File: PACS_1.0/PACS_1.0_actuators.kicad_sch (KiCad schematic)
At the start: 0 parts

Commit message: Finished water pump, cleaned out empty sheets, added details in 'post its'
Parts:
- added D1: GS1M-LTP, symbol Device:D
- added J2: Conn_01x02_Pin, symbol Connector:Conn_01x02_Pin
- added Q2: ~, symbol AOSS32334C:AOSS32334C
- added R4: 1k, symbol Device:R
- added R5: 10k, symbol Device:R
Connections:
- new net: Q2.1, R4.2
- new net: D1.2 (A), J2.1 (Pin_1), Q2.3
- new net +3.3V: D1.1 (K), J2.2 (Pin_2)
- new net GND: Q2.2, R5.1
- new net PWM: R4.1, R5.2
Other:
- note added: "Water Pump Connection"
- company: PACS -> (none)

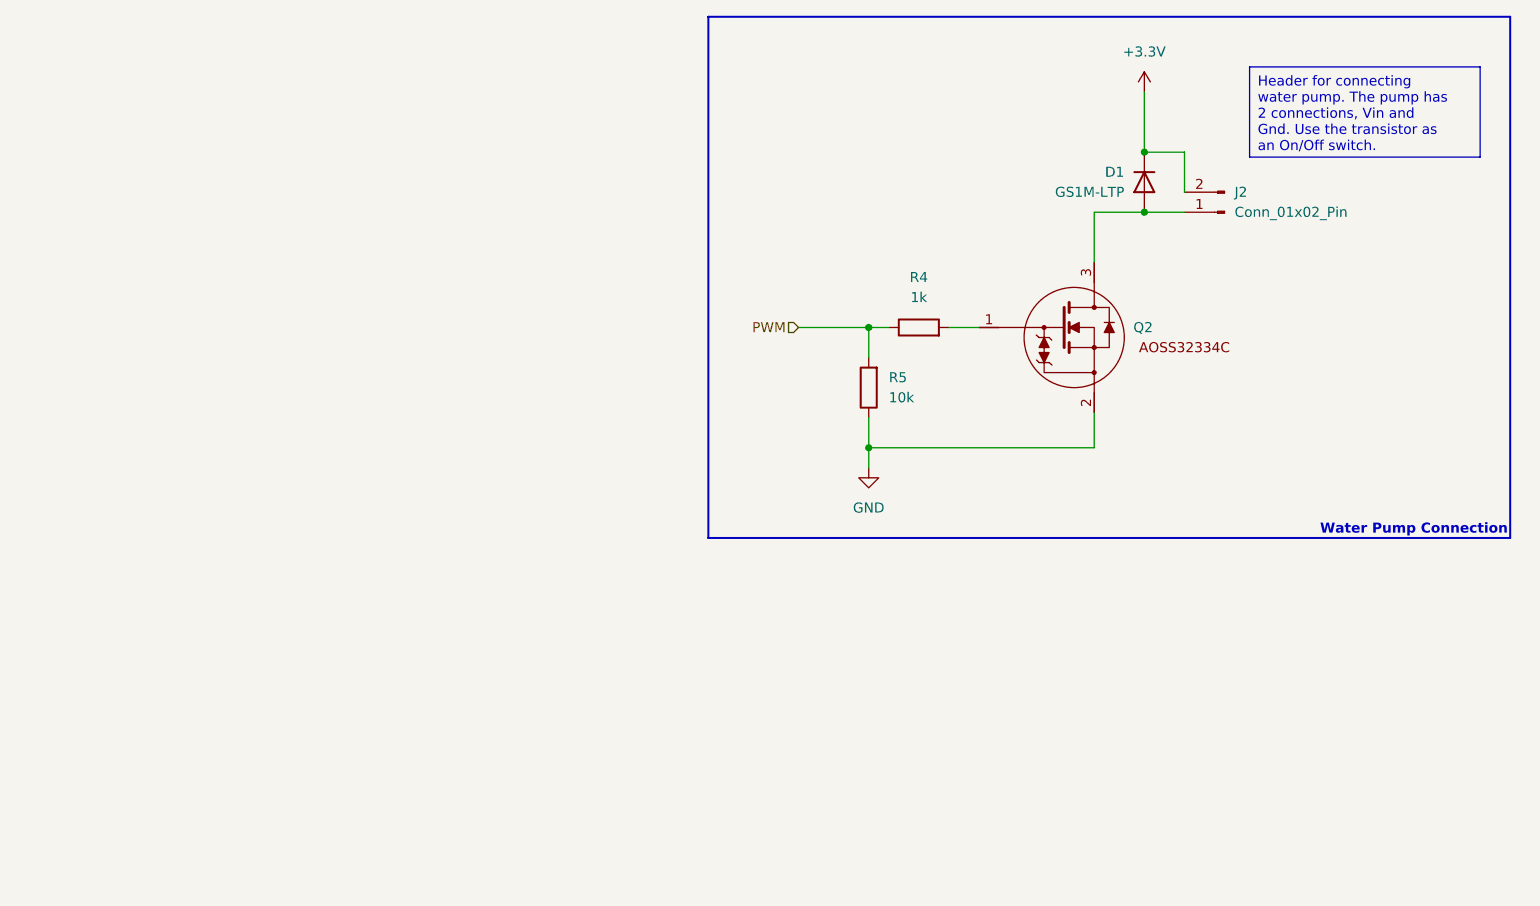
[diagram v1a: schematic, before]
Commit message: Finished Zigbee Module
also fixed some library issues
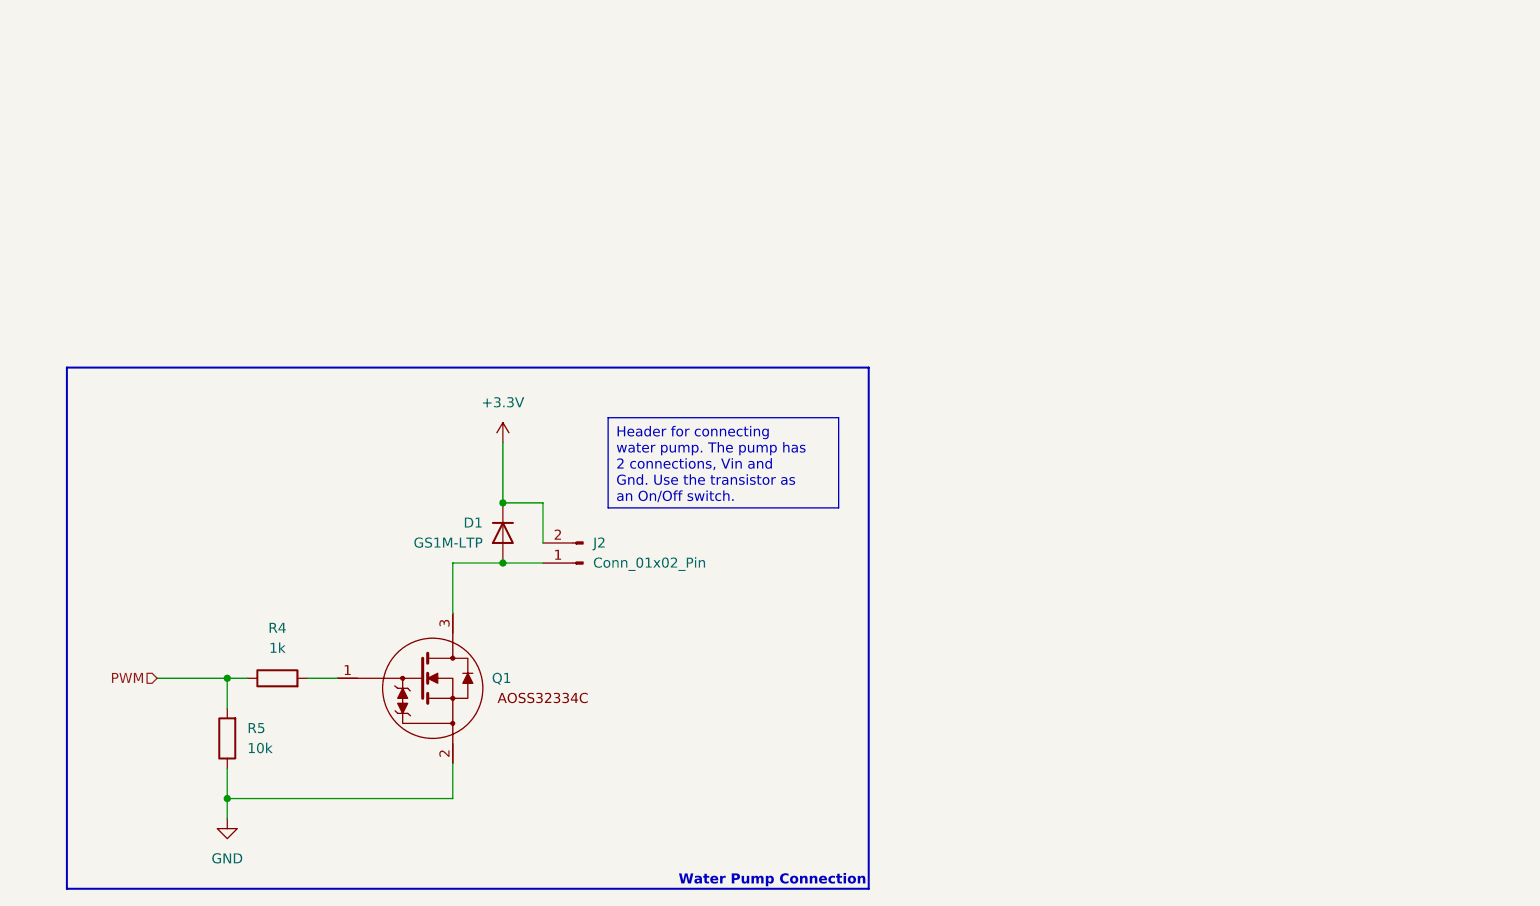
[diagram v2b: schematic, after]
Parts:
- renumbered Q2 to Q1
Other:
- moved on the sheet: D1, J2, Q1, R4, R5

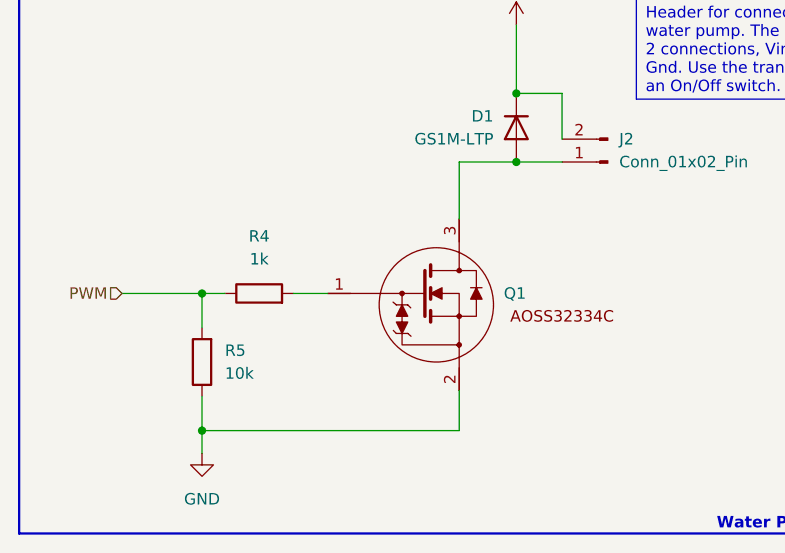
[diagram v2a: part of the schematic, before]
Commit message: Added Undervoltage Protection, removed LED kicad
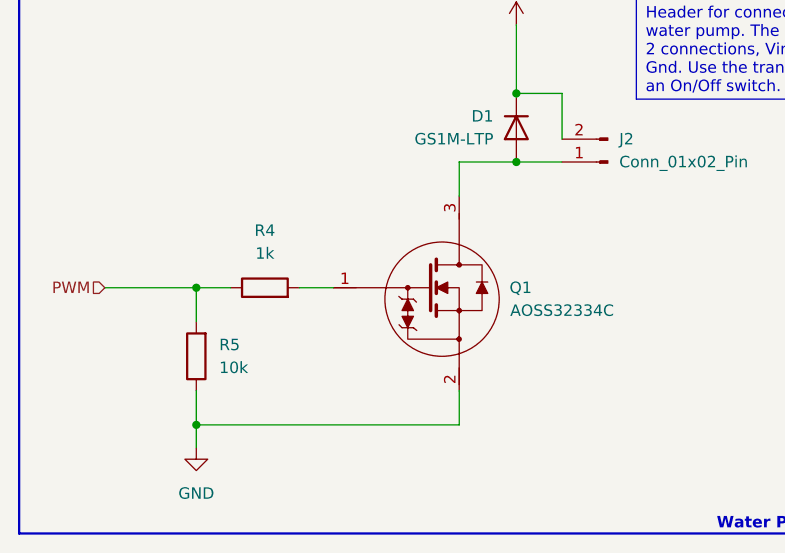
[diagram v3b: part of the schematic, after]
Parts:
- Q1: footprint (none) -> Package_TO_SOT_SMD:TSOT-23; Ref Name (none) -> AOSS32334C
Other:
- moved on the sheet: R4, R5
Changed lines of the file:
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@@
 	(paper "A4")
+	(junction
+		(at 111.76 115.57)
+		(diameter 0)
+		(color 0 0 0 0)
+	)
 	(junction
 		(at 147.32 86.36)
@@
 	)
 	(junction
-		(at 112.395 100.965)
-		(diameter 0)
-		(color 0 0 0 0)
-	)
-	(junction
 		(at 147.32 78.74)
 		(diameter 0)
@@
 	)
 	(junction
-		(at 112.395 116.205)
+		(at 111.76 100.33)
 		(diameter 0)
 		(color 0 0 0 0)
@@
 	(wire
 		(pts
-			(xy 112.395 116.205) (xy 140.97 116.205)
+			(xy 123.19 100.33) (xy 127 100.33)
 		)
 		(stroke
@@
 	(wire
 		(pts
-			(xy 140.97 86.36) (xy 140.97 92.71)
-		)
-		(stroke
-			(width 0)
-			(type default)
-		)
-	)
-	(wire
-		(pts
-			(xy 112.395 112.395) (xy 112.395 116.205)
+			(xy 111.76 115.57) (xy 140.97 115.57)
+		)
+		(stroke
+			(width 0)
+			(type default)
+		)
+	)
+	(wire
+		(pts
+			(xy 111.76 115.57) (xy 111.76 118.11)
 		)
 		(stroke
@@
 	(wire
 		(pts
-			(xy 112.395 100.965) (xy 114.935 100.965)
-		)
-		(stroke
-			(width 0)
-			(type default)
-		)
-	)
-	(wire
-		(pts
-			(xy 122.555 100.965) (xy 126.365 100.965)
-		)
-		(stroke
-			(width 0)
-			(type default)
-		)
-	)
-	(wire
-		(pts
-			(xy 103.505 100.965) (xy 112.395 100.965)
-		)
-		(stroke
-			(width 0)
-			(type default)
-		)
-	)
-	(wire
-		(pts
-			(xy 140.97 111.76) (xy 140.97 116.205)
+			(xy 101.6 100.33) (xy 111.76 100.33)
+		)
+		(stroke
+			(width 0)
+			(type default)
+		)
+	)
+	(wire
+		(pts
+			(xy 140.97 86.36) (xy 140.97 90.17)
+		)
+		(stroke
+			(width 0)
+			(type default)
+		)
+	)
+	(wire
+		(pts
+			(xy 140.97 111.76) (xy 140.97 115.57)
 		)
 		(stroke
@@
 	(wire
 		(pts
-			(xy 112.395 100.965) (xy 112.395 104.775)
-		)
-		(stroke
-			(width 0)
-			(type default)
-		)
-	)
-	(wire
-		(pts
-			(xy 112.395 116.205) (xy 112.395 118.745)
+			(xy 111.76 100.33) (xy 111.76 104.14)
+		)
+		(stroke
+			(width 0)
+			(type default)
+		)
+	)
+	(wire
+		(pts
+			(xy 111.76 111.76) (xy 111.76 115.57)
+		)
+		(stroke
+			(width 0)
+			(type default)
+		)
+	)
+	(wire
+		(pts
+			(xy 111.76 100.33) (xy 115.57 100.33)
 		)
 		(stroke
@@
 	(hierarchical_label "PWM"
 		(shape input)
-		(at 103.505 100.965 180)
+		(at 101.6 100.33 180)
 		(fields_autoplaced yes)
 		(effects
@@
 	(symbol
 		(lib_id "Device:R")
-		(at 112.395 108.585 180)
+		(at 111.76 107.95 180)
 		(unit 1)
 		(exclude_from_sim no)
@@
 		(fields_autoplaced yes)
 		(property "Reference" "R5"
-			(at 114.935 107.3149 0)
+			(at 114.3 106.6799 0)
 			(effects
 				(font
@@
 		)
 		(property "Value" "10k"
-			(at 114.935 109.8549 0)
+			(at 114.3 109.2199 0)
 			(effects
 				(font
@@
 		)
 		(property "Footprint" ""
-			(at 114.173 108.585 90)
+			(at 113.538 107.95 90)
 			(effects
 				(font
@@
 		)
 		(property "Datasheet" "~"
-			(at 112.395 108.585 0)
+			(at 111.76 107.95 0)
 			(effects
 				(font
@@
 		)
 		(property "Description" "Resistor"
-			(at 112.395 108.585 0)
+			(at 111.76 107.95 0)
 			(effects
 				(font
@@
 	(symbol
 		(lib_id "Device:R")
-		(at 118.745 100.965 90)
+		(at 119.38 100.33 90)
 		(unit 1)
 		(exclude_from_sim no)
@@
 		(fields_autoplaced yes)
 		(property "Reference" "R4"
-			(at 118.745 94.615 90)
+			(at 119.38 93.98 90)
 			(effects
 				(font
@@
 		)
 		(property "Value" "1k"
-			(at 118.745 97.155 90)
+			(at 119.38 96.52 90)
 			(effects
 				(font
@@
 		)
 		(property "Footprint" ""
-			(at 118.745 102.743 90)
+			(at 119.38 102.108 90)
 			(effects
 				(font
@@
 		)
 		(property "Datasheet" "~"
-			(at 118.745 100.965 0)
+			(at 119.38 100.33 0)
 			(effects
 				(font
@@
 		)
 		(property "Description" "Resistor"
-			(at 118.745 100.965 0)
+			(at 119.38 100.33 0)
 			(effects
 				(font
@@
 	(symbol
 		(lib_id "AOSS32334C:AOSS32334C")
-		(at 146.685 100.965 0)
+		(at 147.32 100.33 0)
 		(unit 1)
 		(exclude_from_sim no)
@@
 		(dnp no)
 		(property "Reference" "Q1"
-			(at 145.923 100.965 0)
+			(at 146.558 100.33 0)
 			(effects
 				(font
@@
 		)
 		(property "Value" "~"
-			(at 159.385 103.505 0)
+			(at 160.02 102.87 0)
 			(effects
 				(font
@@
 			)
 		)
-		(property "Footprint" ""
-			(at 146.685 100.965 0)
+		(property "Footprint" "Package_TO_SOT_SMD:TSOT-23"
+			(at 147.32 100.33 0)
 			(effects
 				(font
@@
 		)
 		(property "Datasheet" ""
-			(at 146.685 100.965 0)
+			(at 147.32 100.33 0)
 			(effects
 				(font
@@
 		)
 		(property "Description" ""
-			(at 146.685 100.965 0)
-			(effects
-				(font
-					(size 1.27 1.27)
-				)
-				(hide yes)
+			(at 147.32 100.33 0)
+			(effects
+				(font
+					(size 1.27 1.27)
+				)
+				(hide yes)
+			)
+		)
+		(property "Ref Name" "AOSS32334C"
+			(at 152.4 102.87 0)
+			(effects
+				(font
+					(size 1.27 1.27)
+					(color 0 72 72 1)
+				)
 			)
 		)
@@
 	(symbol
 		(lib_id "power:GND")
-		(at 112.395 118.745 0)
+		(at 111.76 118.11 0)
 		(unit 1)
 		(exclude_from_sim no)
@@
 		(fields_autoplaced yes)
 		(property "Reference" "#PWR013"
-			(at 112.395 125.095 0)
+			(at 111.76 124.46 0)
 			(effects
 				(font
@@
 		)
 		(property "Value" "GND"
-			(at 112.395 123.825 0)
+			(at 111.76 123.19 0)
 			(effects
 				(font
@@
 		)
 		(property "Footprint" ""
-			(at 112.395 118.745 0)
+			(at 111.76 118.11 0)
 			(effects
 				(font
@@
 		)
 		(property "Datasheet" ""
-			(at 112.395 118.745 0)
+			(at 111.76 118.11 0)
 			(effects
 				(font
@@
 		)
 		(property "Description" "Power symbol creates a global label with name \"GND\" , ground"
-			(at 112.395 118.745 0)
-			(effects
-				(font
+			(at 111.76 118.11 0)
+			(effects
+				(font

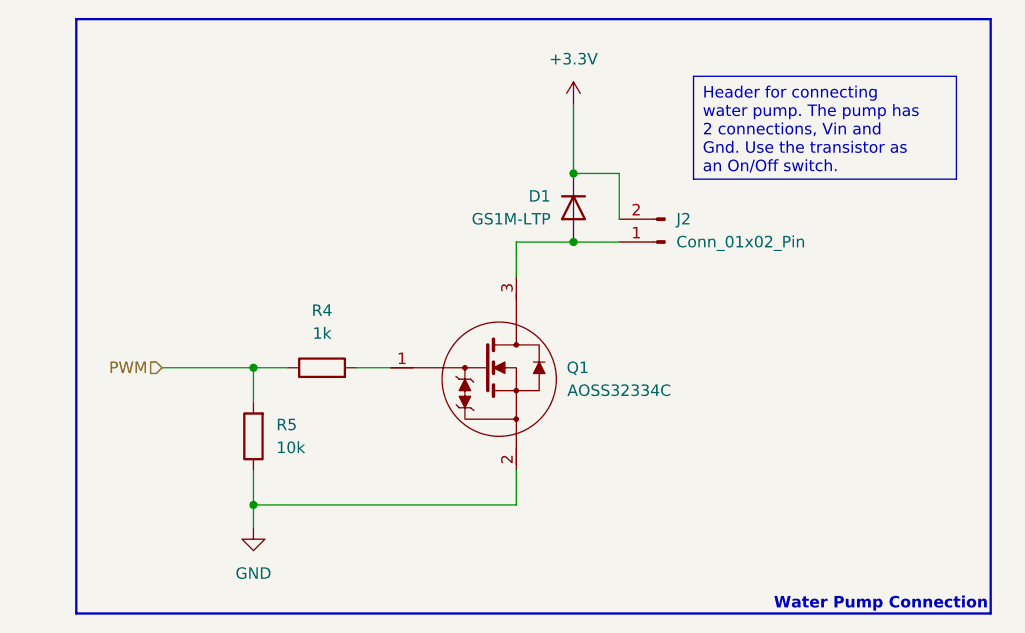
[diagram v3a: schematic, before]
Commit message: Finished 1.0 (NO INA INCLUDED)
Finished PACS 1.0 sheets, Power sheet needs considerations, no INA yet.
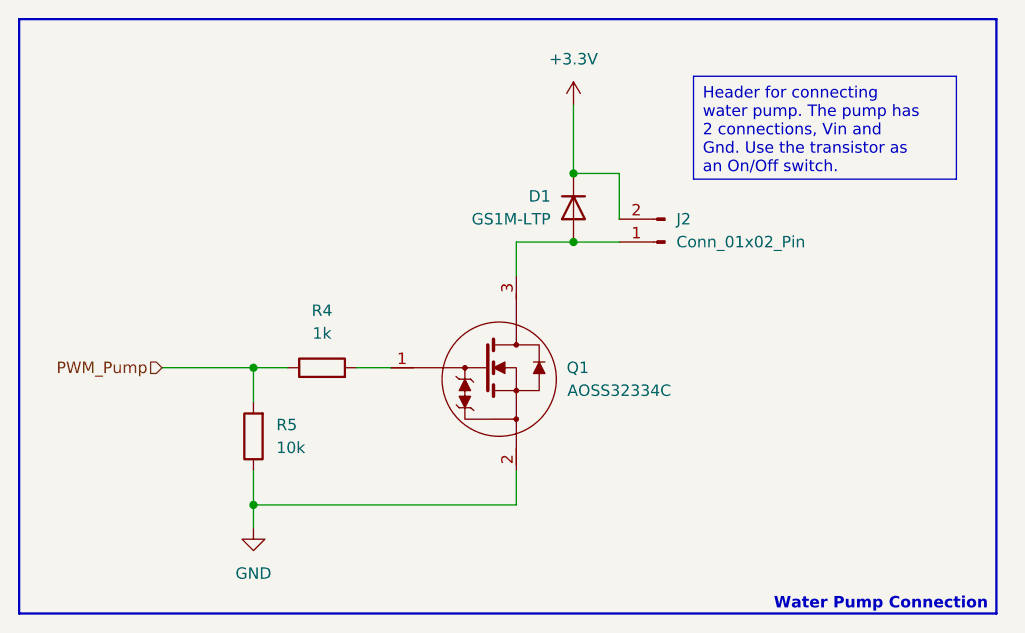
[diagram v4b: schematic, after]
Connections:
- net PWM renamed PWM_Pump
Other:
- company: (none) -> PACS
- title: (none) -> Water Pump
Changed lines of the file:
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@@
 	(generator_version "8.0")
 	(paper "A4")
+	(title_block
+		(title "Water Pump")
+		(date "2024-12-04")
+		(rev "1.0")
+		(company "PACS")
+	)
 	(junction
 		(at 111.76 115.57)
@@
 	)
 	(rectangle
-		(start 92.075 61.595)
-		(end 193.675 127.635)
+		(start 85.725 61.595)
+		(end 194.31 127.635)
 		(stroke
 			(width 0.254)
@@
 		)
 	)
-	(hierarchical_label "PWM"
+	(hierarchical_label "PWM_Pump"
 		(shape input)
 		(at 101.6 100.33 180)

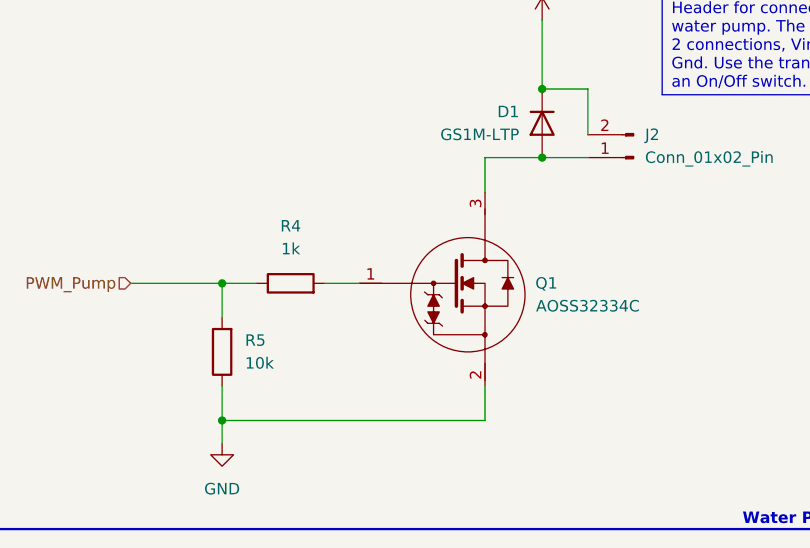
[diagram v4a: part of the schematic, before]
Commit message: Changed reference for Components
C8 to C2 (AS EXAMPLE)
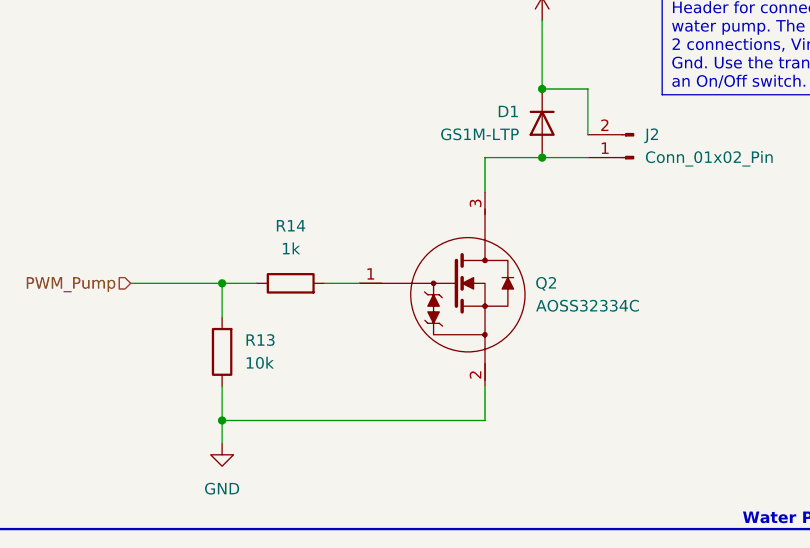
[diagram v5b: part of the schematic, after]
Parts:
- renumbered Q1 to Q2, R5 to R13, R4 to R14
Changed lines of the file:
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@@
 		(dnp no)
 		(fields_autoplaced yes)
-		(property "Reference" "#PWR011"
+		(property "Reference" "#PWR029"
 			(at 147.32 74.93 0)
 			(effects
@@
 			(project "PACS_1.0"
 				(path "/6996cbc8-fffb-40fd-8350-2bb7d19e6e7a/2328e835-669b-4c27-8f58-8619ea15ff21"
-					(reference "#PWR011")
+					(reference "#PWR029")
 					(unit 1)
 				)
@@
 		(dnp no)
 		(fields_autoplaced yes)
-		(property "Reference" "R5"
+		(property "Reference" "R13"
 			(at 114.3 106.6799 0)
 			(effects
@@
 			(project "PACS_1.0"
 				(path "/6996cbc8-fffb-40fd-8350-2bb7d19e6e7a/2328e835-669b-4c27-8f58-8619ea15ff21"
-					(reference "R5")
+					(reference "R13")
 					(unit 1)
 				)
@@
 		(dnp no)
 		(fields_autoplaced yes)
-		(property "Reference" "R4"
+		(property "Reference" "R14"
 			(at 119.38 93.98 90)
 			(effects
@@
 			(project "PACS_1.0"
 				(path "/6996cbc8-fffb-40fd-8350-2bb7d19e6e7a/2328e835-669b-4c27-8f58-8619ea15ff21"
-					(reference "R4")
+					(reference "R14")
 					(unit 1)
 				)
@@
 		(on_board yes)
 		(dnp no)
-		(property "Reference" "Q1"
+		(property "Reference" "Q2"
 			(at 146.558 100.33 0)
 			(effects
@@
 			(project "PACS_1.0"
 				(path "/6996cbc8-fffb-40fd-8350-2bb7d19e6e7a/2328e835-669b-4c27-8f58-8619ea15ff21"
-					(reference "Q1")
+					(reference "Q2")
 					(unit 1)
 				)
@@
 		(dnp no)
 		(fields_autoplaced yes)
-		(property "Reference" "#PWR013"
+		(property "Reference" "#PWR028"
 			(at 111.76 124.46 0)
 			(effects
@@
 			(project "PACS_1.0"
 				(path "/6996cbc8-fffb-40fd-8350-2bb7d19e6e7a/2328e835-669b-4c27-8f58-8619ea15ff21"
-					(reference "#PWR013")
-					(unit 1)
-				)
+					(reference "#PWR028")
+					(unit 1)
+				)

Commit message: Updated footprints for caps and resistors
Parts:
- R13, R14: footprint (none) -> Resistor_SMD:R_0402_1005Metric
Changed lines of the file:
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@@
 			)
 		)
-		(property "Footprint" ""
+		(property "Footprint" "Resistor_SMD:R_0402_1005Metric"
 			(at 113.538 107.95 90)
 			(effects
@@
 			)
 		)
-		(property "Footprint" ""
+		(property "Footprint" "Resistor_SMD:R_0402_1005Metric"
 			(at 119.38 102.108 90)
 			(effects
